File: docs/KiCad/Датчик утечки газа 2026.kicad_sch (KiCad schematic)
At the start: 30 parts, among them J1 Conn_01x04_Pin, J2 Conn_01x04_Pin, Q1 BC846BDW1, Q2 AO4807, U1 TGS_2611-E00, U2 LMR50410, U3 ATtiny412-SS

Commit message: Исправление эл.схемы
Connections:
- net at R7.2: now also U3.3 (PA7); no longer U3.2 (PA6)
- net at R8.2: now also U3.2 (PA6); no longer U3.3 (PA7)

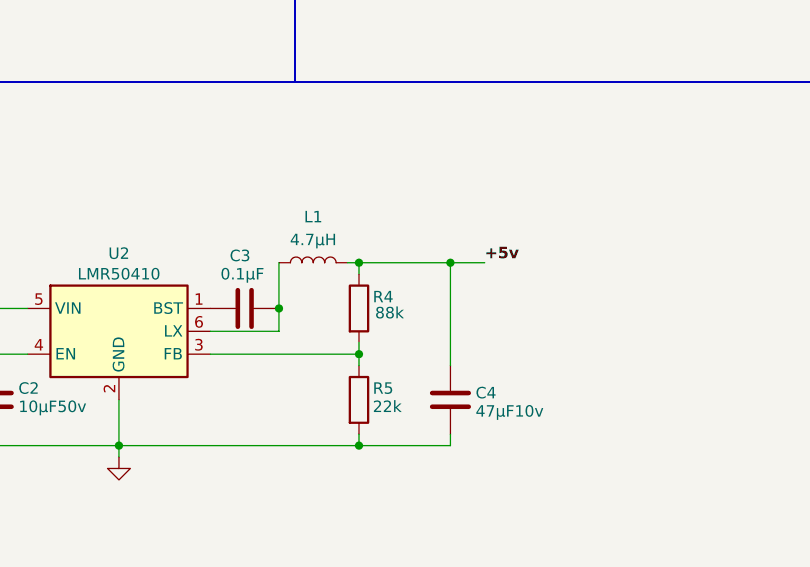
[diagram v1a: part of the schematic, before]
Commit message: Корректировать номиналы схемы питания. Uвых=4,7v
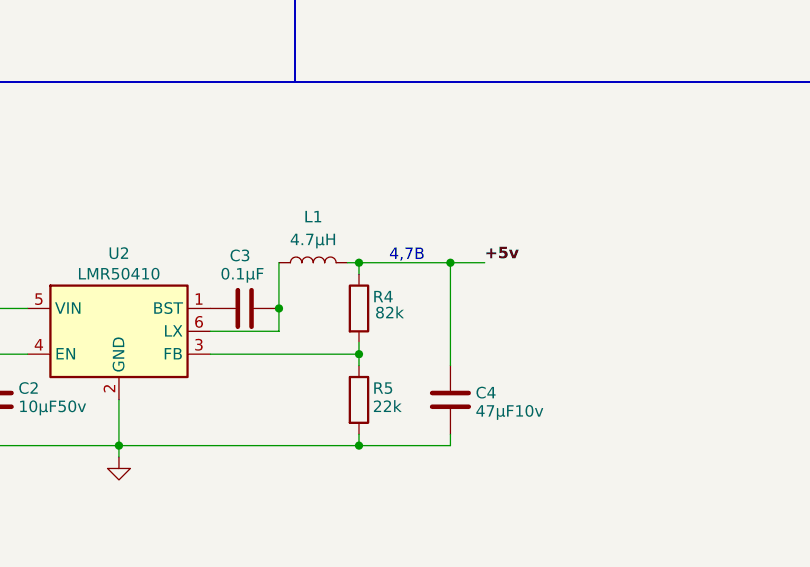
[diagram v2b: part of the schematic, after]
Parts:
- R4: value 88k -> 82k
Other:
- note added: "4,7В"
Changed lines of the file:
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@@
 		)
 	)
+	(text "4,7В"
+		(exclude_from_sim no)
+		(at 134.874 118.618 0)
+		(effects
+			(font
+				(size 1.27 1.27)
+			)
+		)
+	)
 	(text "max 1.5A"
 		(exclude_from_sim no)
@@
 			)
 		)
-		(property "Value" "88k"
+		(property "Value" "82k"
 			(at 131.318 124.968 0)
 			(show_name no)

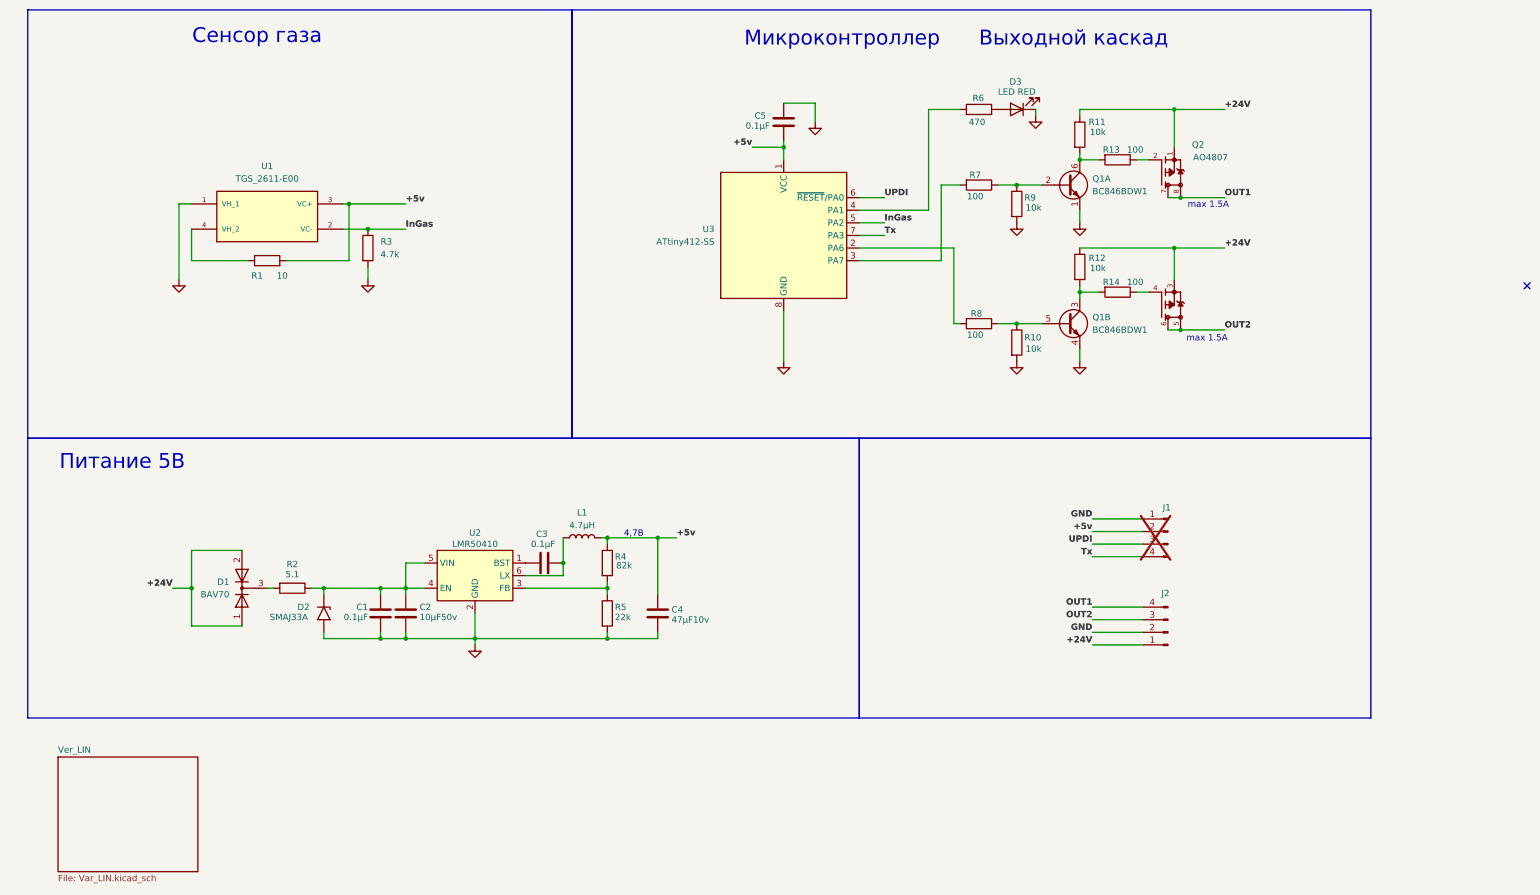
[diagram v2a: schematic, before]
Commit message: Разделить платы разных версий
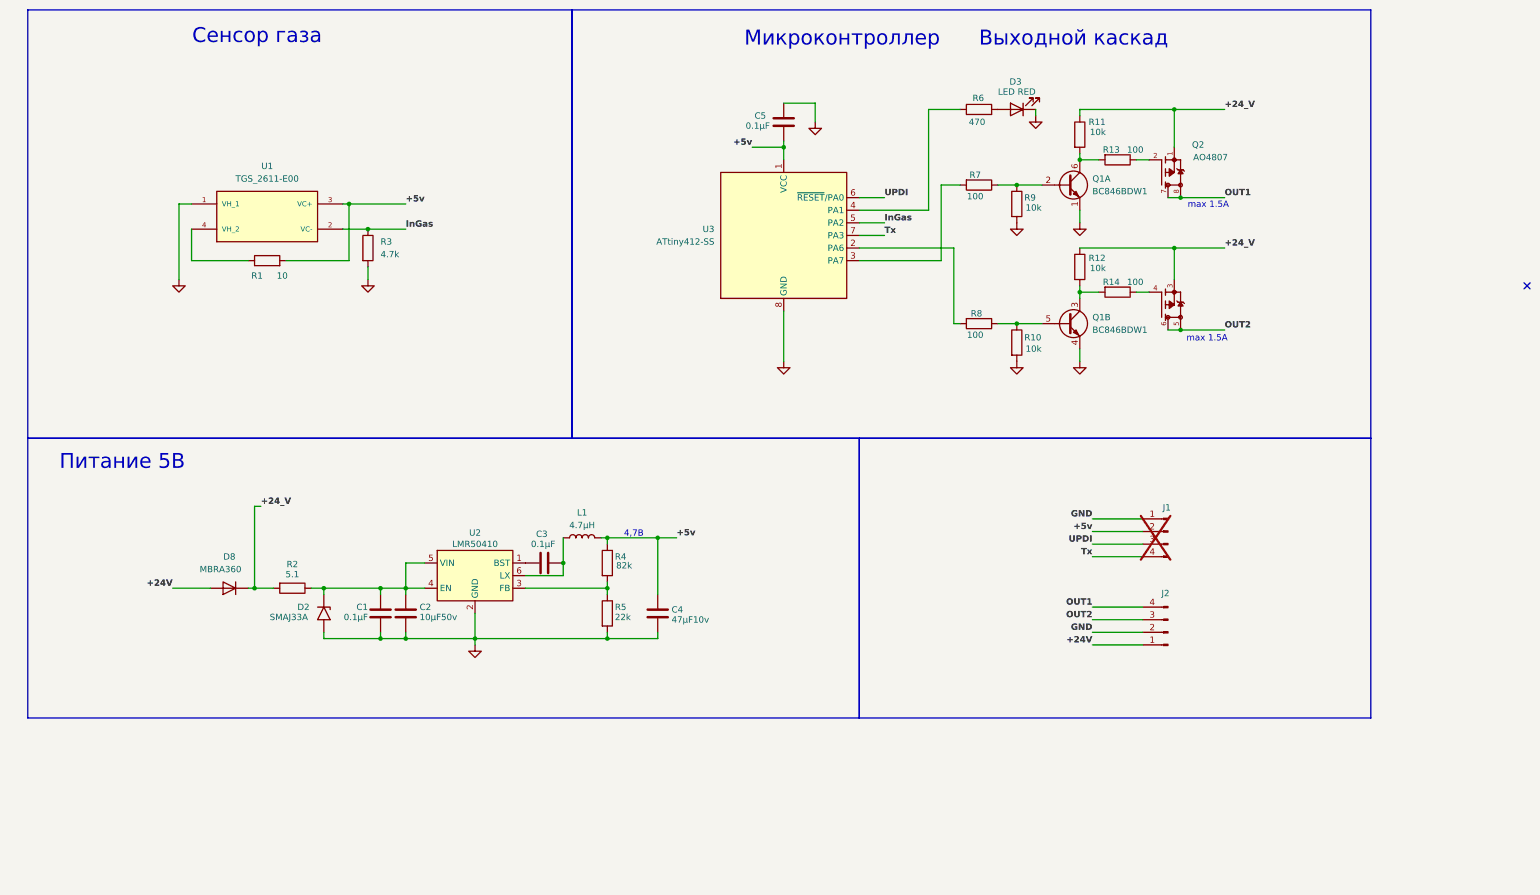
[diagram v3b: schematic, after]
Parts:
- removed D1: BAV70, Package_TO_SOT_SMD:SOT-23, symbol Diode:BAV70
- added D8: MBRA360, Diode_SMD:D_SMA, symbol Device:D
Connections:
- net +24V: now also D8.2 (A); no longer Q2.1, Q2.3, R11.1, R12.1
- net +24_V: now reaches R2.2
- net +24_V: now also Q2.1, Q2.3, R11.1, R12.1, D8.1 (K)
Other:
- removed sheet Ver_LIN
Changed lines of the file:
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@@
 	)
 	(junction
+		(at 58.42 129.54)
+		(diameter 0)
+		(color 0 0 0 0)
+	)
+	(junction
 		(at 83.82 139.7)
 		(diameter 0)
@@
 	)
 	(junction
-		(at 45.72 129.54)
-		(diameter 0)
-		(color 0 0 0 0)
-	)
-	(junction
 		(at 83.82 129.54)
 		(diameter 0)
@@
 	(wire
 		(pts
-			(xy 45.72 137.16) (xy 45.72 129.54)
-		)
-		(stroke
-			(width 0)
-			(type default)
-		)
-	)
-	(wire
-		(pts
 			(xy 83.82 139.7) (xy 88.9 139.7)
 		)
@@
 	(wire
 		(pts
-			(xy 60.96 129.54) (xy 62.23 129.54)
-		)
-		(stroke
-			(width 0)
-			(type default)
-		)
-	)
-	(wire
-		(pts
 			(xy 129.54 129.54) (xy 129.54 128.27)
 		)
@@
 	(wire
 		(pts
+			(xy 58.42 129.54) (xy 62.23 129.54)
+		)
+		(stroke
+			(width 0)
+			(type default)
+		)
+	)
+	(wire
+		(pts
 			(xy 224.79 33.02) (xy 243.84 33.02)
 		)
@@
 	(wire
 		(pts
-			(xy 45.72 129.54) (xy 41.91 129.54)
+			(xy 41.91 129.54) (xy 49.53 129.54)
 		)
 		(stroke
@@
 	(wire
 		(pts
-			(xy 227.33 115.57) (xy 237.49 115.57)
+			(xy 59.69 113.03) (xy 58.42 113.03)
 		)
 		(stroke
@@
 	(wire
 		(pts
-			(xy 45.72 121.92) (xy 45.72 129.54)
+			(xy 227.33 115.57) (xy 237.49 115.57)
 		)
 		(stroke
@@
 	(wire
 		(pts
-			(xy 55.88 121.92) (xy 45.72 121.92)
-		)
-		(stroke
-			(width 0)
-			(type default)
-		)
-	)
-	(wire
-		(pts
-			(xy 55.88 137.16) (xy 45.72 137.16)
-		)
-		(stroke
-			(width 0)
-			(type default)
-		)
-	)
-	(wire
-		(pts
 			(xy 227.33 123.19) (xy 237.49 123.19)
 		)
@@
 	(wire
 		(pts
+			(xy 58.42 113.03) (xy 58.42 129.54)
+		)
+		(stroke
+			(width 0)
+			(type default)
+		)
+	)
+	(wire
+		(pts
 			(xy 64.77 63.5) (xy 77.47 63.5)
 		)
@@
 	(wire
 		(pts
+			(xy 57.15 129.54) (xy 58.42 129.54)
+		)
+		(stroke
+			(width 0)
+			(type default)
+		)
+	)
+	(wire
+		(pts
 			(xy 77.47 52.07) (xy 88.9 52.07)
 		)
@@
 		)
 	)
+	(label "+24_V"
+		(at 59.69 113.03 0)
+		(effects
+			(font
+				(size 1.27 1.27)
+				(thickness 0.254)
+				(bold yes)
+			)
+			(justify left bottom)
+		)
+	)
 	(label "GND"
 		(at 227.33 115.57 180)
@@
 		)
 	)
-	(label "+24V"
-		(at 254 33.02 0)
+	(label "UPDI"
+		(at 185.42 50.8 0)
 		(effects
 			(font
@@
 		)
 	)
-	(label "UPDI"
-		(at 185.42 50.8 0)
+	(label "+24_V"
+		(at 254 60.96 0)
+		(effects
+			(font
+				(size 1.27 1.27)
+				(thickness 0.254)
+				(bold yes)
+			)
+			(justify left bottom)
+		)
+	)
+	(label "+24_V"
+		(at 254 33.02 0)
 		(effects
 			(font
@@
 		)
 	)
-	(label "+24V"
-		(at 254 60.96 0)
-		(effects
-			(font
-				(size 1.27 1.27)
-				(thickness 0.254)
-				(bold yes)
-			)
-			(justify left bottom)
-		)
-	)
 	(label "UPDI"
 		(at 227.33 120.65 180)
@@
 	)
 	(symbol
-		(lib_id "Diode:BAV70")
-		(at 55.88 129.54 90)
+		(lib_id "power:GND")
+		(at 212.09 83.82 0)
 		(unit 1)
 		(body_style 1)
@@
 		(dnp no)
 		(fields_autoplaced yes)
-		(property "Reference" "D1"
-			(at 53.34 128.2699 90)
+		(property "Reference" "#PWR07"
+			(at 212.09 90.17 0)
+			(hide yes)
 			(show_name no)
 			(do_not_autoplace no)
@@
 					(size 1.27 1.27)
 				)
-				(justify left)
 			)
 		)
-		(property "Value" "BAV70"
-			(at 53.34 130.8099 90)
+		(property "Value" "GND"
+			(at 212.09 88.9 0)
+			(hide yes)
 			(show_name no)
 			(do_not_autoplace no)
@@
 					(size 1.27 1.27)
 				)
-				(justify left)
 			)
 		)
-		(property "Footprint" "Package_TO_SOT_SMD:SOT-23"
-			(at 55.88 129.54 0)
+		(property "Footprint" ""
+			(at 212.09 83.82 0)
 			(hide yes)
 			(show_name no)
@@
 			)
 		)
-		(property "Datasheet" "https://assets.nexperia.com/documents/data-sheet/BAV70_SER.pdf"
-			(at 55.88 129.54 0)
+		(property "Datasheet" ""
+			(at 212.09 83.82 0)
 			(hide yes)
 			(show_name no)
@@
 			)
 		)
-		(property "Description" "Dual 100V 215mA high-speed switching diodes, common cathode, SOT-23"
-			(at 55.88 129.54 0)
+		(property "Description" "Power symbol creates a global label with name \"GND\" , ground"
+			(at 212.09 83.82 0)
 			(hide yes)
 			(show_name no)
@@
 			)
 		)
-		(pin "2"
-		)
 		(pin "1"
 		)
-		(pin "3"
-		)
 		(instances
 			(project "Датчик утечки газа 2026"
 				(path "/a17a5c65-2c8f-4811-931f-2f1634edc76c"
-					(reference "D1")
+					(reference "#PWR07")
 					(unit 1)
 				)
@@
 	)
 	(symbol
-		(lib_id "power:GND")
-		(at 212.09 83.82 0)
+		(lib_id "Device:D")
+		(at 53.34 129.54 180)
 		(unit 1)
 		(body_style 1)
@@
 		(in_pos_files yes)
 		(dnp no)
-		(fields_autoplaced yes)
-		(property "Reference" "#PWR07"
-			(at 212.09 90.17 0)
+		(property "Reference" "D8"
+			(at 53.34 123.19 0)
+			(show_name no)
+			(do_not_autoplace no)
+			(effects
+				(font
+					(size 1.27 1.27)
+				)
+			)
+		)
+		(property "Value" "MBRA360"
+			(at 51.562 125.73 0)
+			(show_name no)
+			(do_not_autoplace no)
+			(effects
+				(font
+					(size 1.27 1.27)
+				)
+			)
+		)
+		(property "Footprint" "Diode_SMD:D_SMA"
+			(at 53.34 129.54 0)
 			(hide yes)
 			(show_name no)
@@
 			)
 		)
-		(property "Value" "GND"
-			(at 212.09 88.9 0)
+		(property "Datasheet" ""
+			(at 53.34 129.54 0)
 			(hide yes)
 			(show_name no)
@@
 			)
 		)
-		(property "Footprint" ""
-			(at 212.09 83.82 0)
+		(property "Description" "Diode"
+			(at 53.34 129.54 0)
 			(hide yes)
 			(show_name no)
@@
 			)
 		)
-		(property "Datasheet" ""
-			(at 212.09 83.82 0)
+		(property "Sim.Device" "MBRA360, Диод Шоттки 60В 3А [SMA / DO-214AC]"
+			(at 53.34 129.54 0)
 			(hide yes)
 			(show_name no)
@@
 			)
 		)
-		(property "Description" "Power symbol creates a global label with name \"GND\" , ground"
-			(at 212.09 83.82 0)
+		(property "Sim.Pins" "1=K 2=A"
+			(at 53.34 129.54 0)
 			(hide yes)
 			(show_name no)
@@
 		(pin "1"
 		)
+		(pin "2"
+		)
 		(instances
 			(project "Датчик утечки газа 2026"
 				(path "/a17a5c65-2c8f-4811-931f-2f1634edc76c"
-					(reference "#PWR07")
+					(reference "D8")
 					(unit 1)
 				)
@@
 				)
 			)
-		)
-	)
-	(sheet
-		(at 18.796 163.576)
-		(size 28.194 23.114)
-		(exclude_from_sim no)
-		(in_bom yes)
-		(on_board yes)
-		(dnp no)
-		(fields_autoplaced yes)
-		(stroke
-			(width 0.1524)
-			(type solid)
-		)
-		(fill
-			(color 0 0 0 0)
-		)
-		(property "Sheetname" "Ver_LIN"
-			(at 18.796 162.8644 0)
-			(show_name no)
-			(do_not_autoplace no)
-			(effects
-				(font
-					(size 1.27 1.27)
-				)
-				(justify left bottom)
-			)
-		)
-		(property "Sheetfile" "Var_LIN.kicad_sch"
-			(at 18.796 187.2746 0)
-			(show_name no)
-			(do_not_autoplace no)
-			(effects
-				(font
-					(size 1.27 1.27)
-				)
-				(justify left top)
-			)
-		)
-		(instances
-			(project "Датчик утечки газа 2026"
-				(path "/a17a5c65-2c8f-4811-931f-2f1634edc76c"
-					(page "2")
-				)
-			)
